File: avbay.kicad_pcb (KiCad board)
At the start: 2 copper layers, 28 parts, among them P1 CONN_2, P2 CONN_6, P3 CONN_2, P4 CONN_2, SW1 SW_PUSH, U1 STM32F411RE_LQFP64, U2 XBEE, X1 32.768K, X2 8MHz

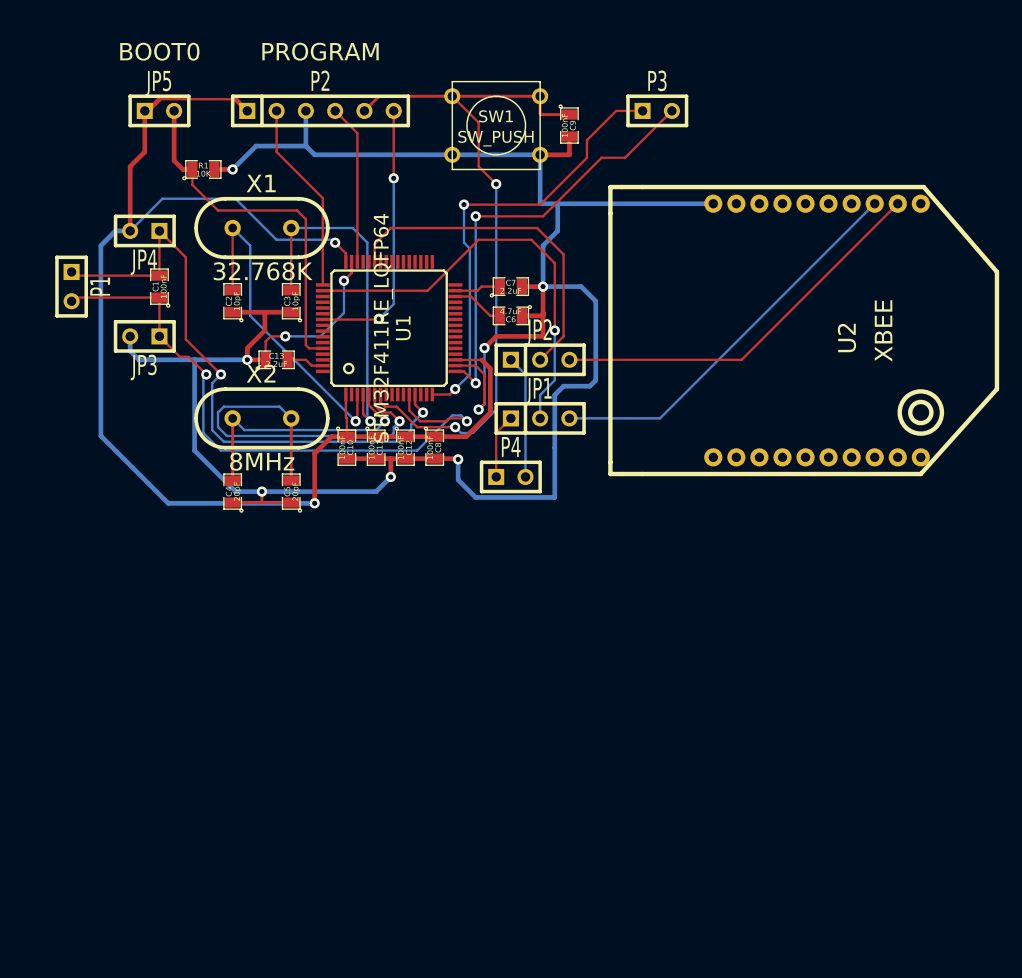
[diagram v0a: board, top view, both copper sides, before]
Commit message: Placed and routed basic PCB
Gonna end up throwing the whole thing out.

Needs to have GPIO headers added because reasons.
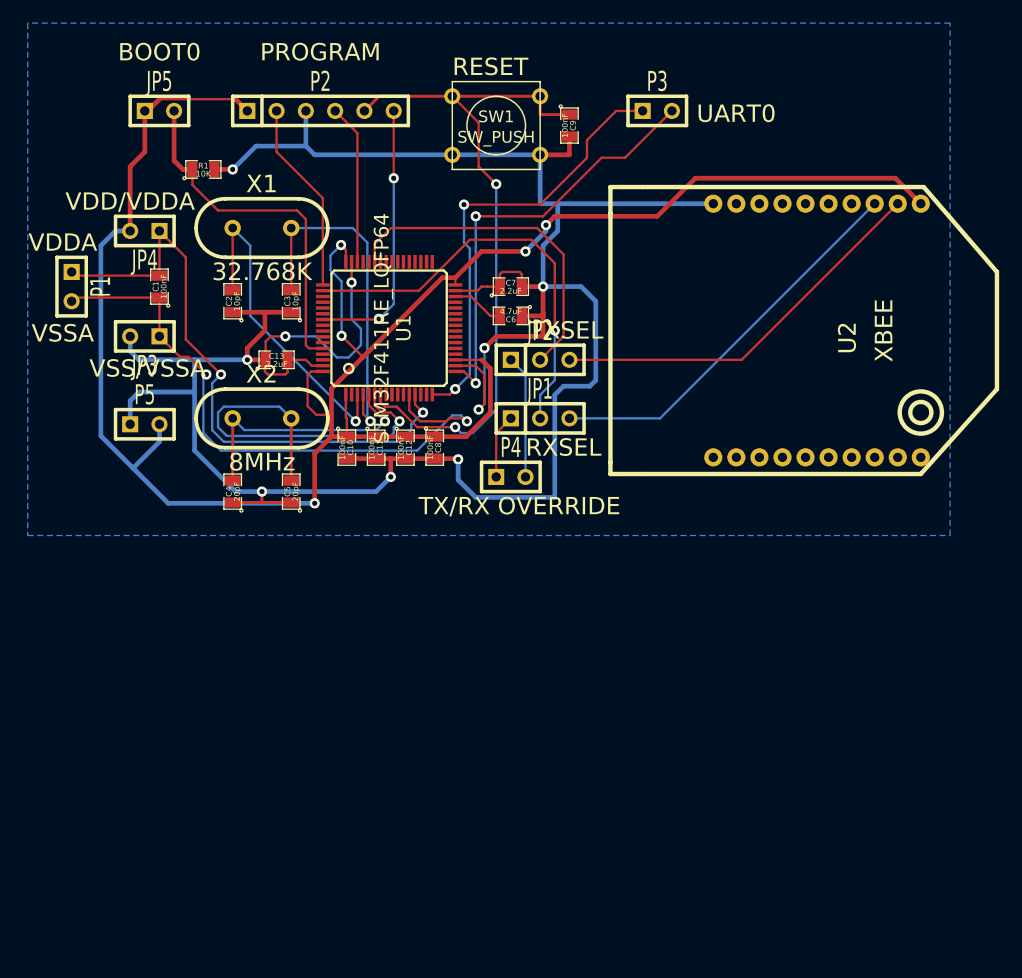
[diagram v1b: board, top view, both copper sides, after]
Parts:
- added P5: CONN_2, SIL-2, F.Cu at (191.8, 126.2)
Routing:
- net 3V3: track 115.7 -> 182.0 mm, vias 2 -> 5
- net GND: track 213.4 -> 234.5 mm
- added copper zone on B.Cu, net GND
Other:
- board text added: "RESET"
- board text added: "RXSEL"
- board text added: "TX/RX OVERRIDE"
- board text added: "TXSEL"
- board text added: "UART0"
- board text added: "VDD/VDDA"
- board text added: "VDDA"
- board text added: "VSS/VSSA"
- board text added: "VSSA"

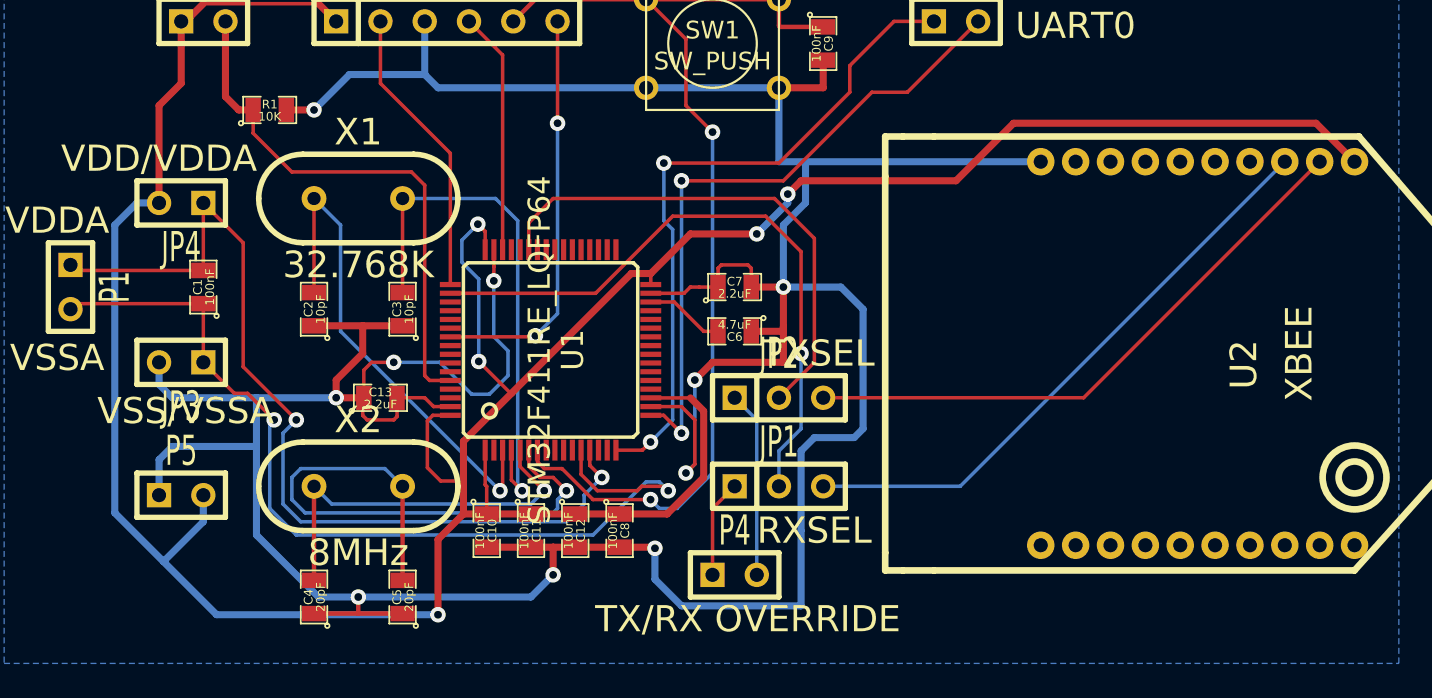
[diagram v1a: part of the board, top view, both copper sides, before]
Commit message: Added voltage regulators
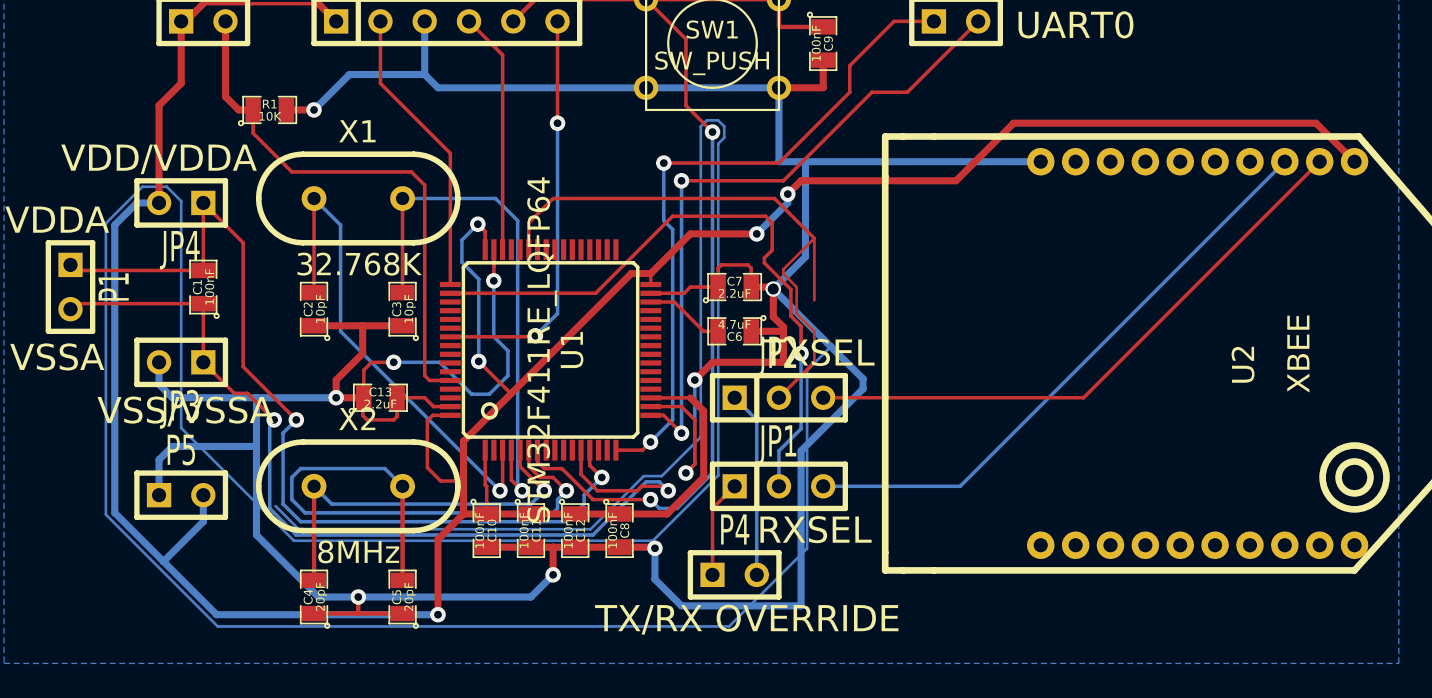
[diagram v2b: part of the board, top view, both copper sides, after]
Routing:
- net GND: track 234.5 -> 425.3 mm
- net /MCU/RADIO_RX: track 29.4 -> 34.5 mm

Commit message: Made breakout board
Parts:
- removed C1: 100nF, SM0805
- removed C13, C7: 2.2uF, SM0805
- removed JP1, JP2: JUMPER3, SIL-3
- removed JP3, JP4, JP5: JUMPER, SIL-2
- removed R1: 10K, SM0805
- removed U2: XBEE, XBee-pro
- added P6: CONN_01X16, Pin_Headers:Pin_Header_Straight_1x16, F.Cu at (209.6, 133.3)
- added P7: CONN_01X16, Pin_Headers:Pin_Header_Straight_1x16, F.Cu at (209.6, 129.5)
- C10, C11, C12, C2, C3, C4, C5, C8, C9: footprint SM0805 -> SMD_Packages:SMD-0805; moved to B.Cu
- C6: footprint SM0805 -> SMD_Packages:SMD-0805
- P1: value CONN_2 -> CONN_01X06; footprint SIL-2 -> Pin_Headers:Pin_Header_Straight_1x06
- P2: value CONN_6 -> CONN_01X06; footprint SIL-6 -> Pin_Headers:Pin_Header_Straight_1x06
- P3: value CONN_2 -> CONN_01X04; footprint SIL-2 -> Pin_Headers:Pin_Header_Straight_1x04
- P4, P5: value CONN_2 -> CONN_01X16; footprint SIL-2 -> Pin_Headers:Pin_Header_Straight_1x16
- SW1: footprint SW_PUSH_SMALL -> Discret:SW_PUSH_SMALL
- U1: footprint LQFP64 -> Housings_QFP:LQFP-64_10x10mm_Pitch0.5mm
- X1, X2: footprint HC-49V -> Discret:HC-49V
- moved P3 71.2 mm to (195.6, 157.5)
- moved SW1 57.2 mm to (224.8, 157.5)
- moved C9 57.2 mm to (228.6, 157.5)
- moved P2 50.0 mm to (227.3, 144.8), turned to 90 degrees
- moved P1 48.8 mm to (223.5, 144.8), turned to 90 degrees
- moved P5 42.7 mm to (209.6, 165.1)
- moved P4 40.6 mm to (209.6, 168.9)
- moved X1 31.1 mm to (195.6, 139.7)
- moved U1 29.6 mm to (209.6, 147.3)
- moved C6 28.1 mm to (218.9, 144.6)
- moved C2 27.4 mm to (193.0, 142.2)
- moved C3 27.4 mm to (198.1, 142.2)
- moved C11 25.5 mm to (201.9, 151.8), turned to 90 degrees
- moved X2 25.0 mm to (195.6, 149.9)
- moved C8 23.8 mm to (217.2, 152.1)
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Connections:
- C2 pad 2: N-0000036 -> Net-(C2-Pad2)
- C3 pad 2: N-0000035 -> Net-(C3-Pad2)
- C4 pad 2: N-0000034 -> Net-(C4-Pad2)
- C5 pad 2: N-0000033 -> Net-(C5-Pad2)
- C6 pad 2: N-0000038 -> Net-(C6-Pad2)
- P1 pad 1: /MCU/VDDA -> GND
- P1 pad 2: /MCU/VSSA -> GND
- P3 pad 1: /MCU/USART_TX -> /MCU/RADIO_TX
- P3 pad 2: /MCU/USART_RX -> /MCU/RADIO_RX
- P4 pad 1: /OVERRIDE_TX -> 3V3
- P4 pad 2: /OVERRIDE_RX -> /MCU/PC13
- P5 pad 1: GND -> /MCU/USART_RX
- P5 pad 2: 3V3 -> GND
- U1 pad 10: (no net) -> /MCU/PC2
- U1 pad 11: (no net) -> /MCU/PC3
- U1 pad 12: /MCU/VSSA -> Net-(P4-Pad12)
- U1 pad 14: (no net) -> /MCU/PA0
- U1 pad 15: (no net) -> /MCU/PA1
- U1 pad 2: (no net) -> /MCU/PC13
- U1 pad 20: (no net) -> /MCU/PA4
- U1 pad 21: (no net) -> /MCU/PA5
- U1 pad 22: (no net) -> /MCU/PA6
- U1 pad 23: (no net) -> /MCU/PA7
- U1 pad 24: (no net) -> /MCU/PC4
- U1 pad 25: (no net) -> /MCU/PC5
- U1 pad 26: (no net) -> /MCU/PB0
- U1 pad 27: (no net) -> /MCU/PB1
- U1 pad 28: (no net) -> /MCU/PB2
- U1 pad 29: (no net) -> /MCU/PB10
- U1 pad 3: N-0000036 -> Net-(C2-Pad2)
- U1 pad 30: N-0000038 -> Net-(C6-Pad2)
- U1 pad 33: (no net) -> /MCU/PB12
- U1 pad 34: (no net) -> /MCU/PB13
- U1 pad 35: (no net) -> /MCU/PB14
- U1 pad 36: (no net) -> /MCU/PB15
- U1 pad 37: (no net) -> /MCU/PC6
- U1 pad 38: (no net) -> /MCU/PC7
- U1 pad 39: (no net) -> /MCU/PC8
- U1 pad 4: N-0000035 -> Net-(C3-Pad2)
- U1 pad 40: (no net) -> /MCU/PC9
- U1 pad 41: (no net) -> /MCU/PA8
- U1 pad 42: (no net) -> /MCU/RADIO_TX
- U1 pad 44: (no net) -> /MCU/PA11
- U1 pad 45: (no net) -> /MCU/PA12
- U1 pad 5: N-0000034 -> Net-(C4-Pad2)
- U1 pad 50: /MCU/RADIO_TX -> /MCU/PA15
- U1 pad 51: (no net) -> /MCU/PC10
- U1 pad 52: (no net) -> /MCU/PC11
- U1 pad 53: (no net) -> /MCU/PC12
- U1 pad 54: (no net) -> /MCU/PD2
- U1 pad 56: (no net) -> /MCU/PB4
- U1 pad 57: (no net) -> /MCU/PB5
- U1 pad 58: (no net) -> /MCU/PB6
- U1 pad 59: (no net) -> /MCU/PB7
- U1 pad 6: N-0000033 -> Net-(C5-Pad2)
- U1 pad 61: (no net) -> /MCU/PB8
- U1 pad 62: (no net) -> /MCU/PB9
- U1 pad 8: (no net) -> /MCU/PC0
- U1 pad 9: (no net) -> /MCU/PC1
- X1 pad 1: N-0000036 -> Net-(C2-Pad2)
- X1 pad 2: N-0000035 -> Net-(C3-Pad2)
- X2 pad 1: N-0000034 -> Net-(C4-Pad2)
- X2 pad 2: N-0000033 -> Net-(C5-Pad2)
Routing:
- net GND: track 425.3 -> 191.6 mm, vias 10 -> 7
- net 3V3: track 182.0 -> 307.8 mm, vias 5 -> 7
- net /MCU/VSSA: track 53.7 -> 0.00 mm, vias 2 -> 0
- net Net-(C2-Pad2): track 0.00 -> 43.7 mm
- net /MCU/USART_TX: track 38.7 -> 80.2 mm, vias 2 -> 0
- net Net-(C3-Pad2): track 0.00 -> 41.0 mm
- net Net-(C4-Pad2): track 0.00 -> 39.7 mm, vias 0 -> 1
- net /MCU/PA15: track 0.00 -> 37.3 mm, vias 0 -> 1
- net Net-(C5-Pad2): track 0.00 -> 34.9 mm, vias 0 -> 1
- net /MCU/PC10: track 0.00 -> 34.8 mm, vias 0 -> 1
- net /MCU/JTCK-SWCLK: track 16.8 -> 51.4 mm, vias 0 -> 1
- net N-0000033: track 34.2 -> 0.00 mm, vias 1 -> 0
- net /XBEE_RX: track 34.2 -> 0.00 mm
- net /XBEE_TX: track 34.1 -> 0.00 mm
- net /MCU/VDDA: track 53.3 -> 20.6 mm, vias 2 -> 0
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- added copper zone on F.Cu, net 3V3
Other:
- board outline added: 44.5 x 45.7 mm
- net class Default: via_dia 0.889 -> 0.7112; via_drill 0.635 -> 0.3302
- net class Power: via_dia 0.889 -> 0.7112; via_drill 0.635 -> 0.3302
- board text added: "1"
- board text added: "16"
- board text added: "17"
- board text added: "32"
- board text added: "33"
- board text added: "3v3"
- board text added: "48"
- board text added: "49"
- board text added: "64"
- board text added: "DEBUG"
- board text added: "GND"
- board text added: "RX1"
- board text added: "RX2"
- board text added: "TX1"
- board text added: "TX2"
- board text removed: "BOOT0"
- board text removed: "PROGRAM"
- board text removed: "RXSEL"
- board text removed: "TX/RX OVERRIDE"
- board text removed: "TXSEL"
- board text removed: "UART0"
- board text removed: "VDD/VDDA"
- board text removed: "VDDA"
- board text removed: "VSS/VSSA"
- board text removed: "VSSA"
